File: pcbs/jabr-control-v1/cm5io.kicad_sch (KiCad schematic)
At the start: 5 parts, among them J10001 ARJM11D7-502-AB-EW2, J10002 TYPE-C-31-M-12, U2401 PESD4USB3BTTS-QX, U2402 PESD4USB3BTTS-QX

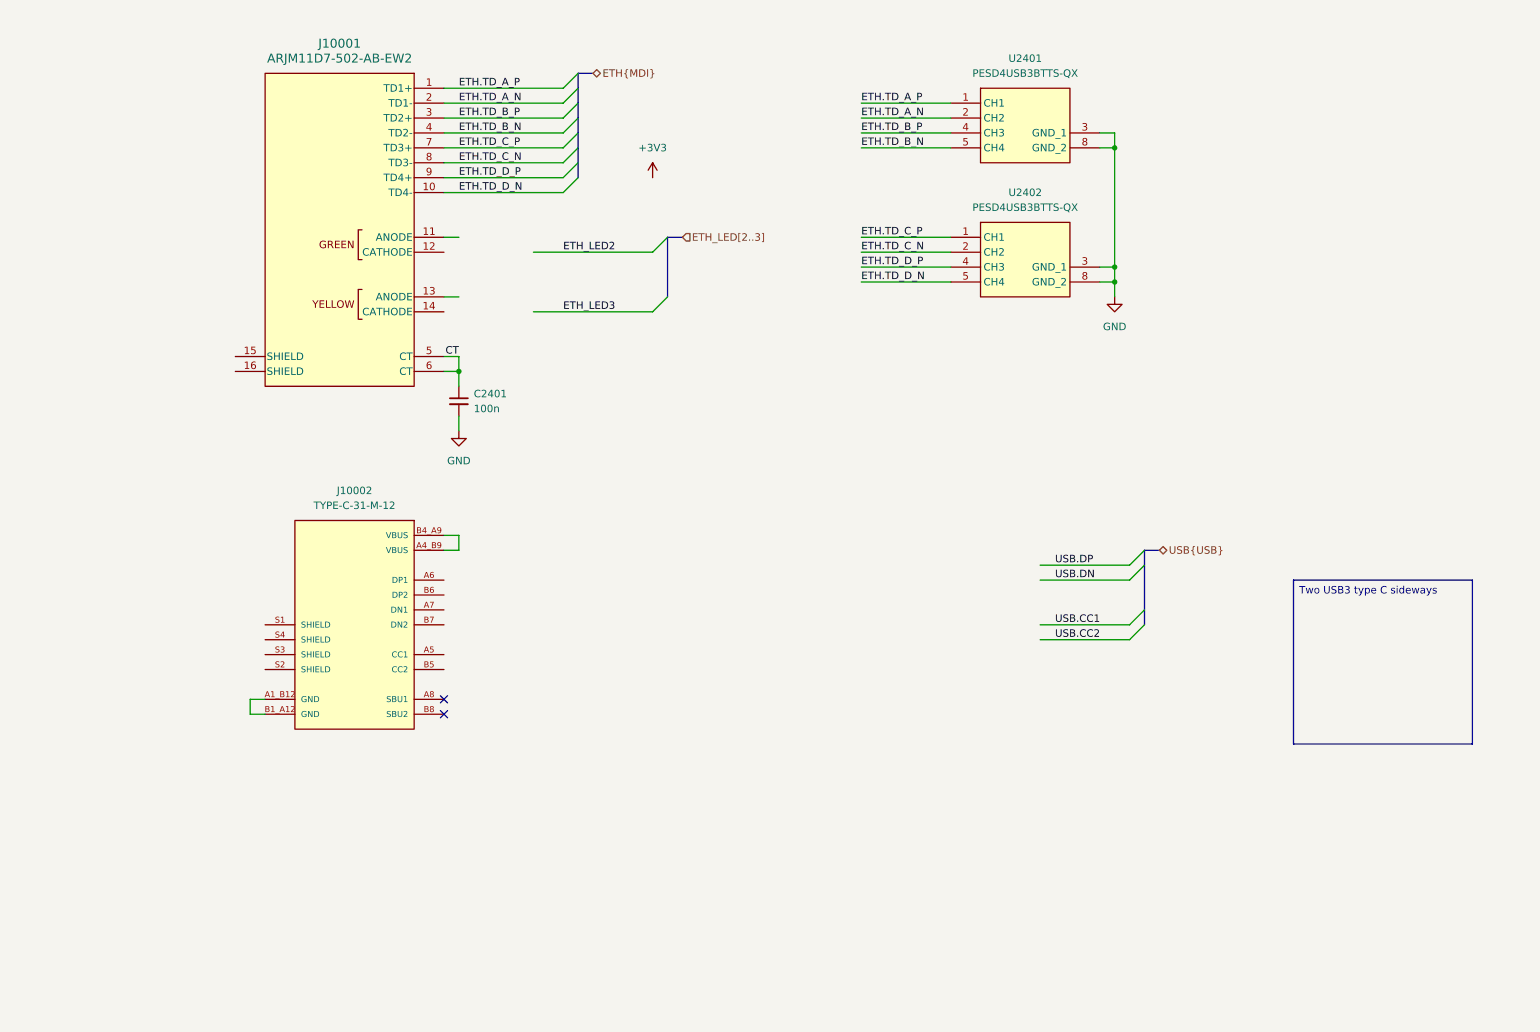
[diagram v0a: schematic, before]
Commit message: Schematic nearing completion, need to do GPIO and PHY decouplings caps
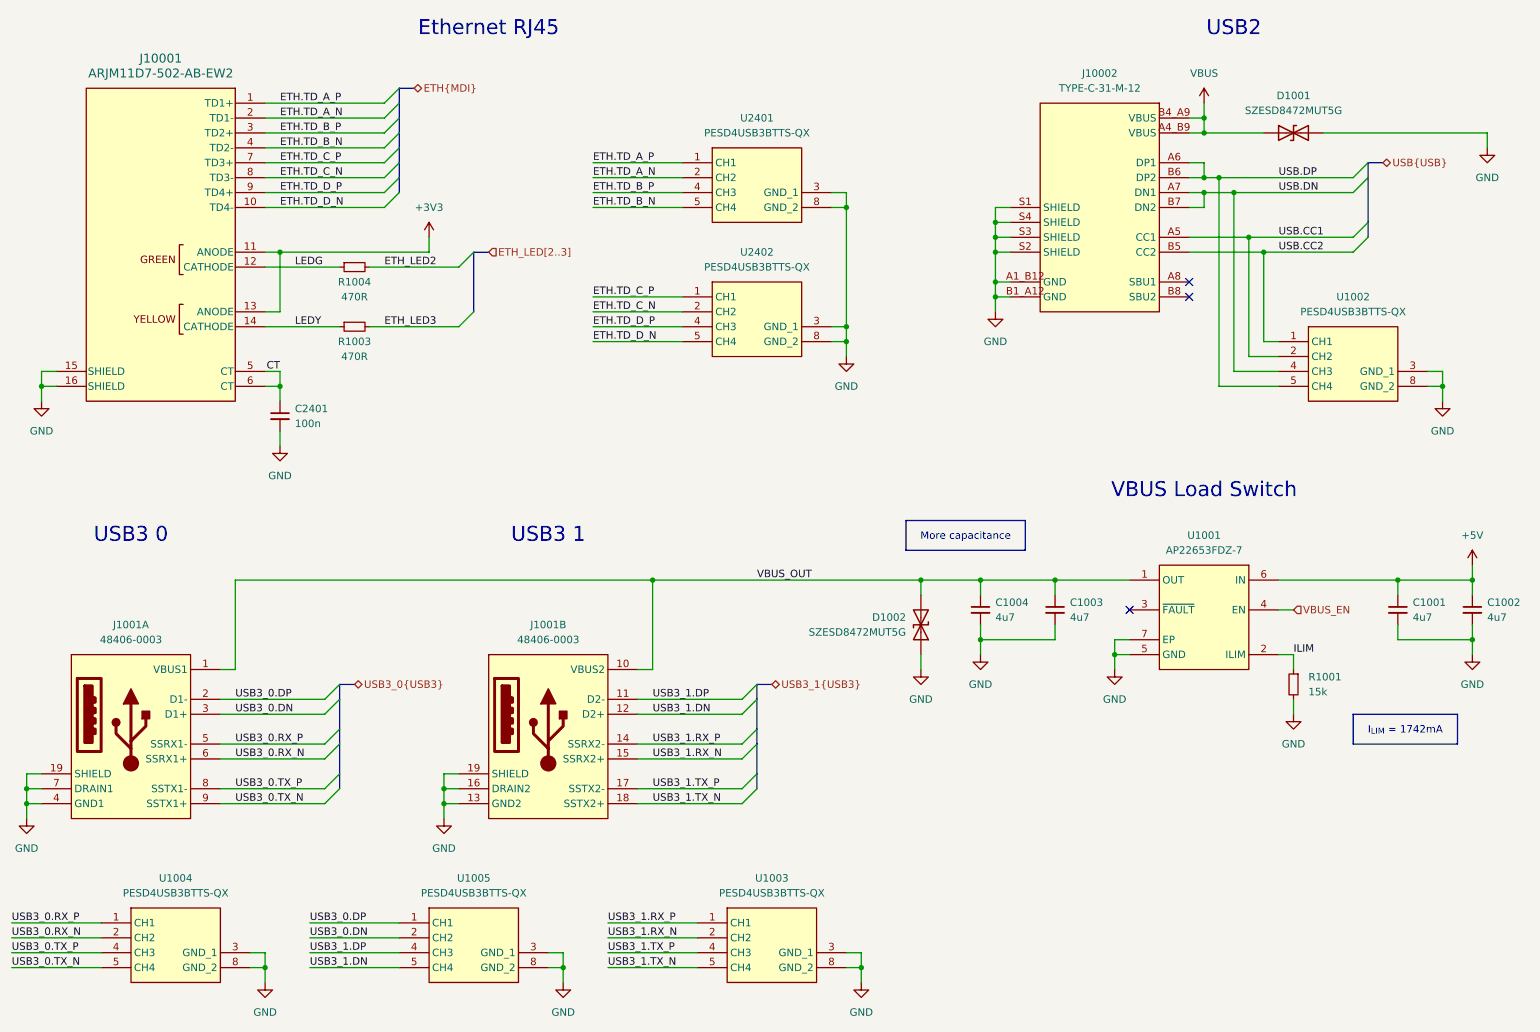
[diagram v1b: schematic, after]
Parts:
- added C1001, C1002, C1003, C1004: 4u7, project_footprints:C_0402, symbol DEV:C_SMALL
- added D1001, D1002: SZESD8472MUT5G, project_footprints:SZESD7462N2T5G, symbol TVS:SZESD8472MUT5G
- added J1001: 48406-0003, project_footprints:48406-0003, symbol USB-CONN:48406-0003
- added R1001: 15k, symbol DEV:R_SMALL
- added R1003, R1004: 470R, symbol DEV:R_SMALL
- added U1001: AP22653FDZ-7, project_footprints:SON65P200X200X80-7N-D, symbol PWR-SWCH:AP22653FDZ-7
- added U1002, U1003, U1004, U1005: PESD4USB3BTTS-QX, project_footprints:PESD4USB3BTTSQX, symbol TVS:PESD4USB3BTTS-QX
- C2401: footprint Capacitor_SMD:C_0402_1005Metric -> project_footprints:C_0402; symbol Device:C_Small -> DEV:C_SMALL
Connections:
- net +3V3: now also J10001.11 (ANODE), J10001.13 (ANODE)
- net ETH_LED2: now also R1004.2
- net ETH_LED3: now also R1003.2
- net GND: now also J10001.15 (SHIELD), J10001.16 (SHIELD), J10002.A1_B12 (GND), J10002.B1_A12 (GND), J10002.S1 (SHIELD), J10002.S2 (SHIELD), J10002.S3 (SHIELD), J10002.S4 (SHIELD), C1001.2, C1002.2, C1003.2, C1004.2, D1001.2 (A2), D1002.1 (A1), J1001.13 (GND2), J1001.16 (DRAIN2), J1001.19 (SHIELD), J1001.19 (SHIELD), J1001.4 (GND1), J1001.7 (DRAIN1), R1001.2, U1001.5 (GND), U1001.7 (EP), U1002.3 (GND_1), U1002.8 (GND_2), U1003.3 (GND_1), U1003.8 (GND_2), U1004.3 (GND_1), U1004.8 (GND_2), U1005.3 (GND_1), U1005.8 (GND_2)
- net USB.CC1: now also J10002.A5 (CC1), U1002.2 (CH2), U1002.9 (NC)
- net USB.CC2: now also J10002.B5 (CC2), U1002.1 (CH1), U1002.10 (NC)
- net USB.DN: now also J10002.A7 (DN1), J10002.B7 (DN2), U1002.4 (CH3), U1002.7 (NC)
- net USB.DP: now also J10002.A6 (DP1), J10002.B6 (DP2), U1002.5 (CH4), U1002.6 (NC)
- net VBUS: now reaches J10002.A4_B9 (VBUS), J10002.B4_A9 (VBUS)
- net VBUS: now also D1001.1 (A1)
- net LEDG: now reaches J10001.12 (CATHODE)
- net LEDG: now also R1004.1
- net LEDY: now reaches J10001.14 (CATHODE)
- net LEDY: now also R1003.1
- new net +5V: C1001.1, C1002.1, U1001.6 (IN)
- new net ILIM: R1001.1, U1001.2 (ILIM)
- new net USB3_0.DN: J1001.3 (D1+), U1005.2 (CH2), U1005.9 (NC)
- new net USB3_0.DP: J1001.2 (D1-), U1005.1 (CH1), U1005.10 (NC)
- new net USB3_0.RX_N: J1001.6 (SSRX1+), U1004.2 (CH2), U1004.9 (NC)
- new net USB3_0.RX_P: J1001.5 (SSRX1-), U1004.1 (CH1), U1004.10 (NC)
- new net USB3_0.TX_N: J1001.9 (SSTX1+), U1004.5 (CH4), U1004.6 (NC)
- new net USB3_0.TX_P: J1001.8 (SSTX1-), U1004.4 (CH3), U1004.7 (NC)
- new net USB3_1.DN: J1001.12 (D2+), U1005.5 (CH4), U1005.6 (NC)
- new net USB3_1.DP: J1001.11 (D2-), U1005.4 (CH3), U1005.7 (NC)
- new net USB3_1.RX_N: J1001.15 (SSRX2+), U1003.2 (CH2), U1003.9 (NC)
- new net USB3_1.RX_P: J1001.14 (SSRX2-), U1003.1 (CH1), U1003.10 (NC)
- new net USB3_1.TX_N: J1001.18 (SSTX2+), U1003.5 (CH4), U1003.6 (NC)
- new net USB3_1.TX_P: J1001.17 (SSTX2-), U1003.4 (CH3), U1003.7 (NC)
- new net VBUS_EN: U1001.4 (EN)
- new net VBUS_OUT: C1003.1, C1004.1, D1002.2 (A2), J1001.1 (VBUS1), J1001.10 (VBUS2), U1001.1 (OUT)
- no-connect marks 2 -> 3
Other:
- note added: "Ethernet RJ45"
- note added: "USB2"
- note added: "USB3 0"
- note added: "USB3 1"
- note added: "VBUS Load Switch"
- moved on the sheet: C2401, J10001, J10002, U2401, U2402
